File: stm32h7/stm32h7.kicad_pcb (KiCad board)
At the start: 4 copper layers, 46.9 x 47 mm, 23 parts, among them J1 Conn_02x18_Counter_Clockwise, J2 Conn_02x18_Counter_Clockwise, J3 Conn_02x18_Counter_Clockwise, J4 Conn_02x18_Counter_Clockwise, SW1 SW_SPDT, U1 STM32H743ZITx, Y1 ABM3-8.000MHZ

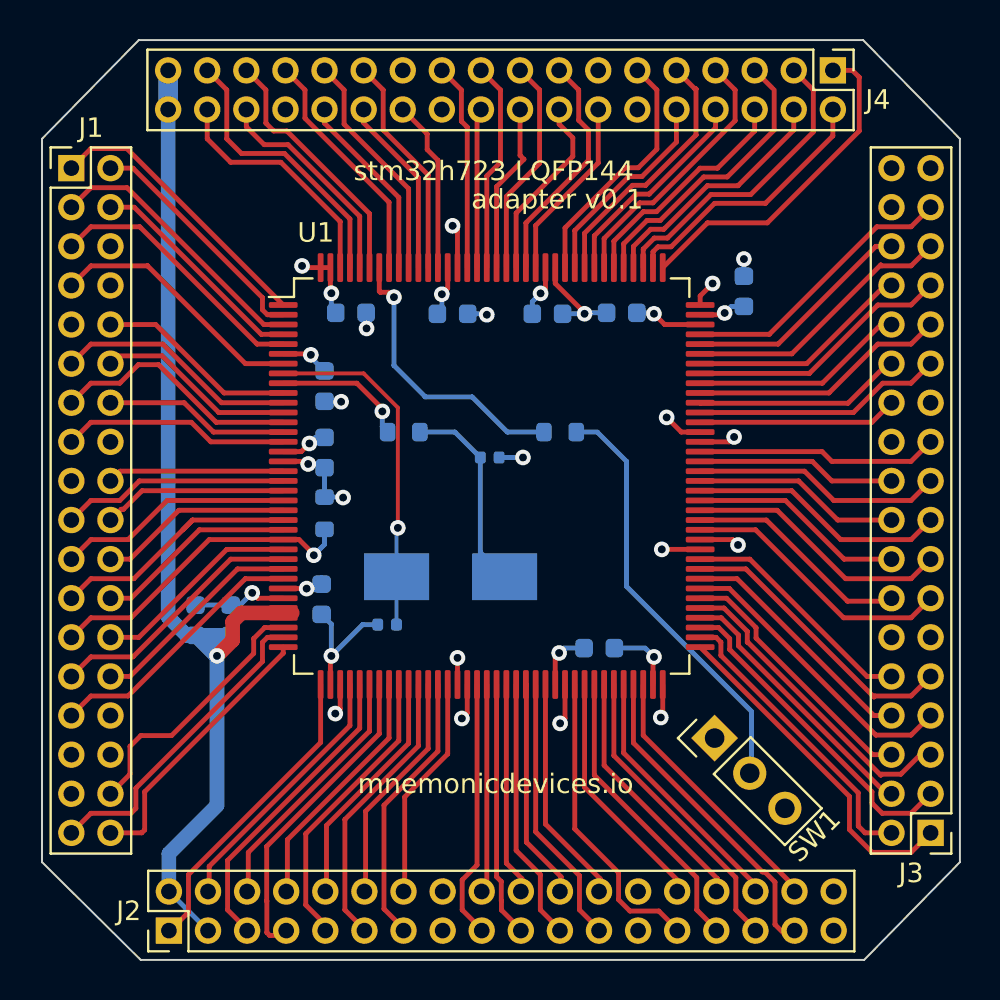
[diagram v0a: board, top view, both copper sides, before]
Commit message: add gerber for stm32h7
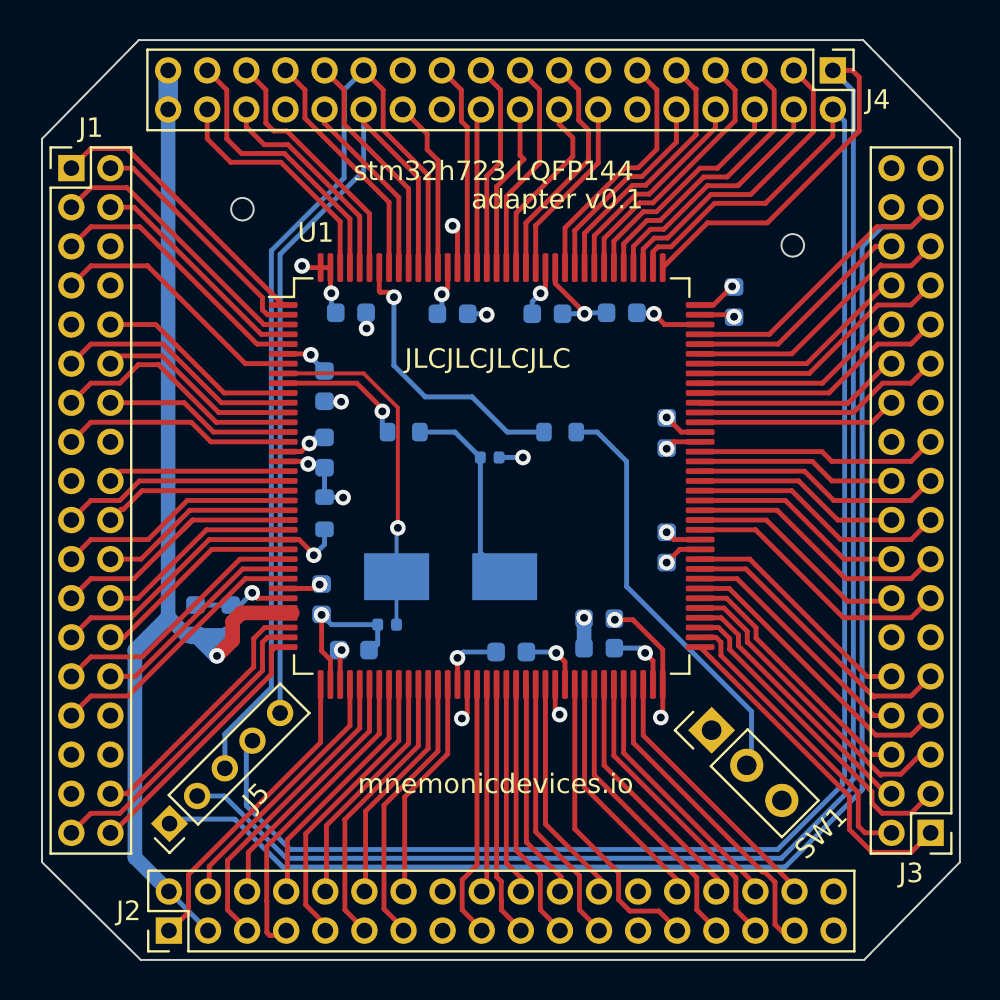
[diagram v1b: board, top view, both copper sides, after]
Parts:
- added C14: 100n, Capacitor_SMD:C_0603_1608Metric, B.Cu at (28.1, 43.2)
- added C15: 100n, Capacitor_SMD:C_0603_1608Metric, B.Cu at (44.0, 38.0)
- added C16: 100n, Capacitor_SMD:C_0603_1608Metric, B.Cu at (36.1, 43.3)
- added C17: 100n, Capacitor_SMD:C_0603_1608Metric, B.Cu at (40.6, 41.6)
- added C18: 100n, Capacitor_SMD:C_0603_1608Metric, B.Cu at (44.0, 32.1)
- added J5: Conn_01x05, Connector_PinHeader_2.00mm:PinHeader_1x05_P2.00mm_Vertical, F.Cu at (18.6, 52.1)
- moved C1 0.74 mm to (47.5, 25.4)
- moved SW1 0.43 mm to (46.4, 47.3)
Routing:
- net 109: track 17.2 -> 90.7 mm
- net 110: track 13.8 -> 84.9 mm
- net 105: track 14.5 -> 84.8 mm
- net 133: track 11.5 -> 50.1 mm
- net 134: track 9.25 -> 41.9 mm
- net +3V3: track 40.6 -> 46.1 mm
- net GND: track 57.3 -> 60.4 mm, vias 14 -> 15
- net +3.3VA: track 55.6 -> 58.0 mm
- net 36: track 14.1 -> 13.5 mm
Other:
- outline, holes or cut-outs redrawn
- board text added: "JLCJLCJLCJLC"

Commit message: update stm32h7 gerber and assembly
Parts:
- moved C7 0.81 mm to (27.8, 25.1)
- moved C9 0.80 mm to (33.1, 25.2)
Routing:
- net +3V3: track 46.1 -> 44.4 mm
- net GND: track 60.4 -> 58.9 mm, vias 15 -> 16
- net 124: track 9.58 -> 9.00 mm

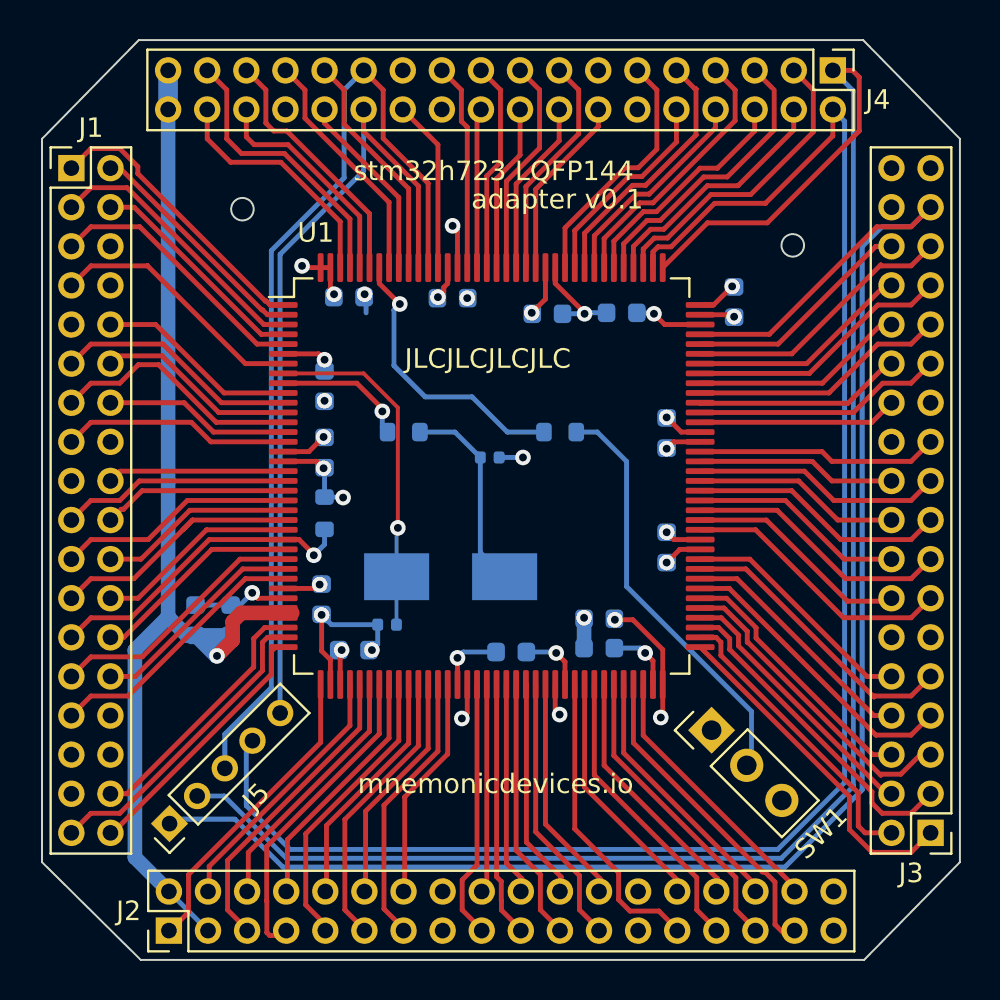
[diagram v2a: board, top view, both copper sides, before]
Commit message: add dedicated symbol and footprint for easier porting
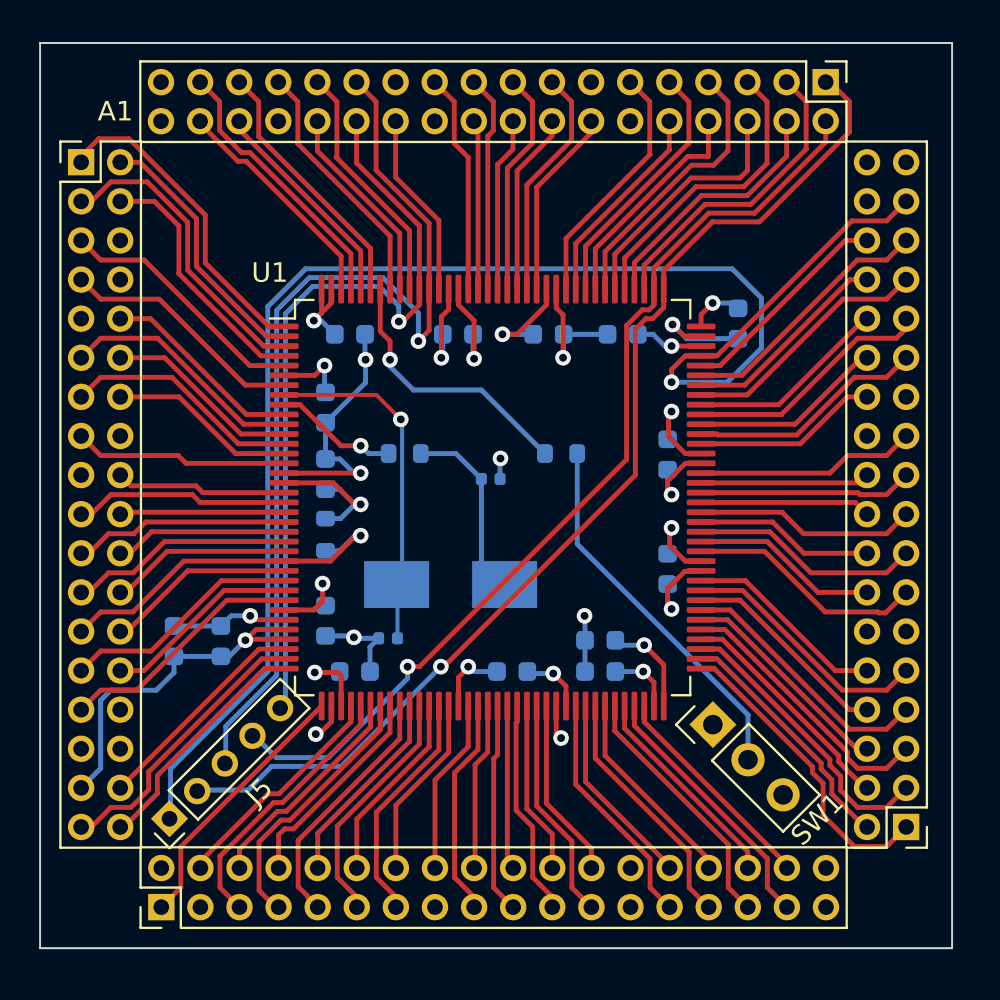
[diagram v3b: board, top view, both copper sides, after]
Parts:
- removed J1, J2, J3, J4: Conn_02x18_Counter_Clockwise, Connector_PinHeader_2.00mm:PinHeader_2x18_P2.00mm_Vertical
- added A1: Adapter, Connector_PinHeader_2.00mm:stm32h7_adapter, F.Cu at (35.2, 36.2)
- moved C7 1.90 mm to (27.9, 27.1)
- moved C9 1.87 mm to (33.4, 27.1)
- moved C12 1.54 mm to (18.9, 42.8)
- moved C8 1.20 mm to (40.6, 44.3)
- moved C13 1.19 mm to (21.2, 42.8)
- moved C1 1.12 mm to (47.7, 26.5)
- moved C6 1.12 mm to (26.6, 41.7)
- moved C18 1.10 mm to (44.1, 33.2)
- moved C11 1.10 mm to (26.6, 30.8)
- moved C5 1.10 mm to (26.6, 34.2)
- moved C10 1.10 mm to (41.8, 27.1)
- moved C17 1.10 mm to (40.6, 42.7)
- moved C4 1.10 mm to (35.0, 34.5)
- moved R1 1.10 mm to (30.6, 33.1)
- moved R2 1.10 mm to (38.6, 33.1)
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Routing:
- net +3.3VA: track 58.0 -> 18.3 mm
- net 110: track 84.9 -> 49.3 mm, vias 0 -> 1
- net 109: track 90.7 -> 55.9 mm, vias 0 -> 1
- net +3V3: track 44.4 -> 64.3 mm, vias 16 -> 12
- net 105: track 84.8 -> 79.0 mm, vias 0 -> 1
- net 63: track 15.6 -> 12.3 mm
- net 69: track 16.6 -> 13.5 mm
- net 43: track 16.3 -> 13.6 mm
- net 74: track 15.3 -> 12.7 mm
- net 58: track 11.3 -> 8.83 mm
- net 65: track 15.2 -> 12.7 mm
- net 66: track 13.0 -> 10.5 mm
- net 60: track 11.7 -> 9.24 mm
- net 56: track 10.9 -> 8.41 mm
- net 70: track 13.8 -> 11.3 mm
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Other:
- board size 46.9 x 47 mm -> 46.6 x 46.3 mm
- board text removed: "JLCJLCJLCJLC"
- board text removed: "adapter v0.1"
- board text removed: "mnemonicdevices.io"
- board text removed: "stm32h723 LQFP144"

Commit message: update stm32h7 adapter
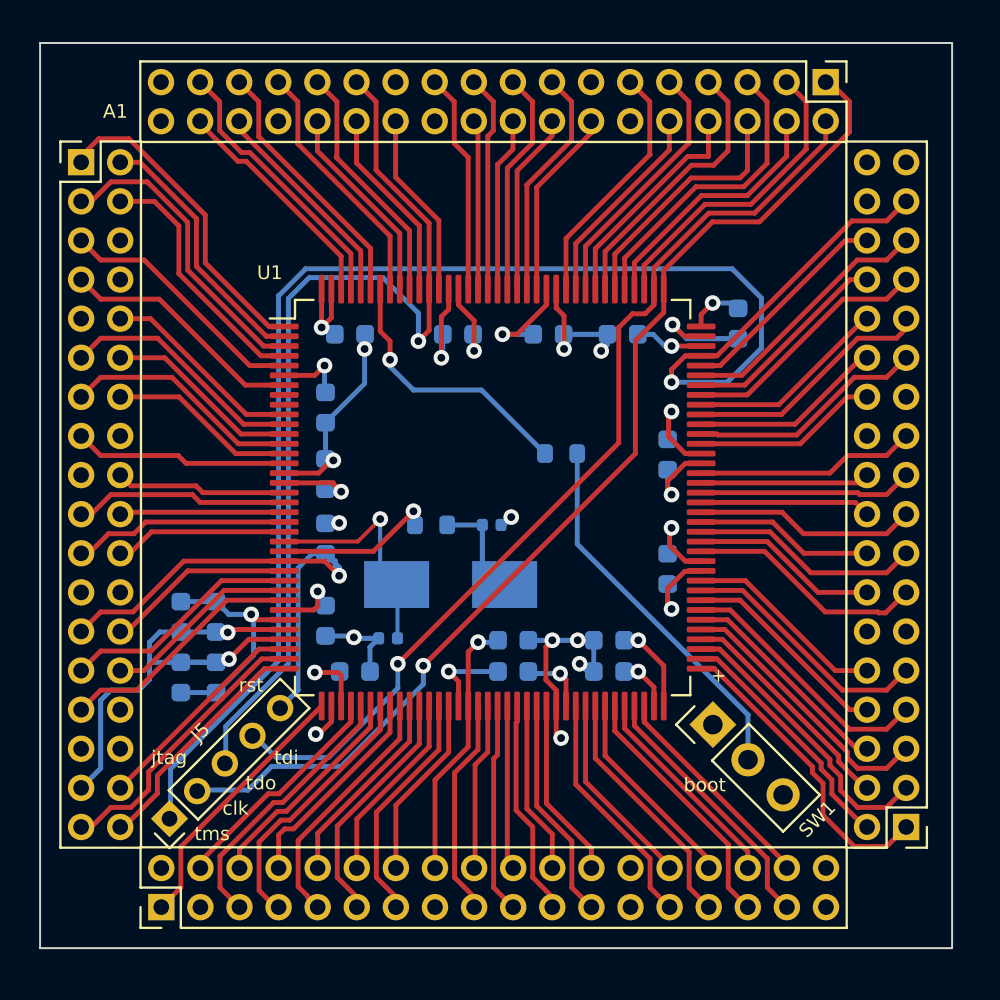
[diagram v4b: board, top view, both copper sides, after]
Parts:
- removed R3: 10k, Resistor_SMD:R_0603_1608Metric
- added C19: 100n, Capacitor_SMD:C_0603_1608Metric, B.Cu at (26.6, 37.5)
- added C20: 100n, Capacitor_SMD:C_0603_1608Metric, B.Cu at (36.2, 42.7)
- added C21: 1u, Capacitor_SMD:C_0603_1608Metric, B.Cu at (21.0, 44.6)
- added C22: 100n, Capacitor_SMD:C_0603_1608Metric, B.Cu at (19.2, 44.6)
- moved R1 3.89 mm to (32.0, 36.8)
- moved C4 2.35 mm to (35.1, 36.8)
- moved C12 1.30 mm to (19.2, 41.5)
- moved C13 1.27 mm to (21.0, 41.5)
- moved C17 0.45 mm to (41.1, 42.7)
- moved C8 0.45 mm to (41.1, 44.3)
- moved C16 0.05 mm to (36.2, 44.3)
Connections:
- net 105 renamed JTAG_TMS
- net 109 renamed JTAG_CLK
- net 110 renamed JTAG_TDI
- net 133 renamed JTAG_TDO
- A1 pad 23: 23 -> GND
- A1 pad 24: 24 -> GND
- A1 pad 25: 25 -> NRST
- J5 pad 5: 134 -> NRST
- U1 pad 23: 23 -> /HSE_IN
- U1 pad 24: 24 -> /HSE_OUT
- U1 pad 25: 25 -> NRST
- U1 pad 8: /HSE_IN -> (no net)
- U1 pad 9: /HSE_OUT -> (no net)
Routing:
- net 134: track 39.9 -> 9.92 mm, vias 1 -> 0
- net NRST: track 0.00 -> 26.8 mm, vias 0 -> 1
- net 25: track 18.0 -> 0.00 mm, vias 1 -> 0
- net GND: track 60.7 -> 72.5 mm, vias 14 -> 18
- net 23: track 11.5 -> 0.00 mm
- net 24: track 9.26 -> 0.00 mm
- net +3.3VA: track 18.3 -> 25.1 mm, vias 1 -> 2
- net /HSE_IN: track 17.8 -> 11.9 mm
- net Net-(C4-Pad2): track 9.53 -> 5.32 mm
- net /HSE_OUT: track 6.37 -> 8.19 mm
- net Net-(U1-Pad71): track 3.42 -> 2.39 mm
- net +3V3: track 64.3 -> 63.8 mm, vias 12 -> 13
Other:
- board text added: "+"
- board text added: "boot"
- board text added: "clk"
- board text added: "jtag"
- board text added: "rst"
- board text added: "tdi"
- board text added: "tdo"
- board text added: "tms"
